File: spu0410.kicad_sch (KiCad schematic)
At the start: 10 parts, among them U1601 LT6233CS6#TRMPBF

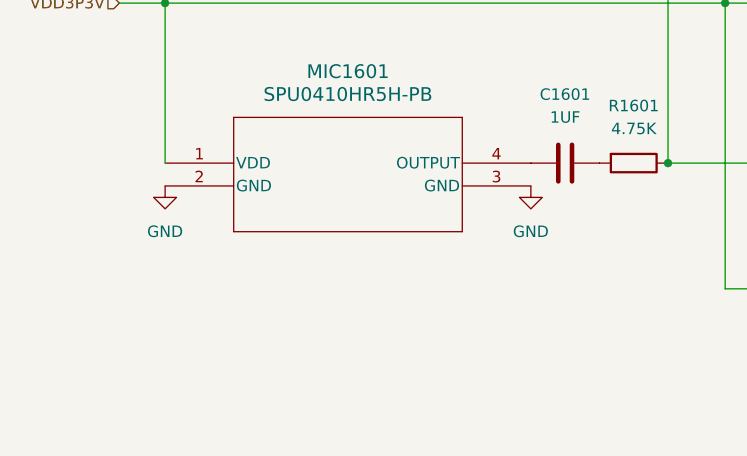
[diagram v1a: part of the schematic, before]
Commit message: Added -3.3V supply, buffer amplifier, and single-to-differential op-amp circuit
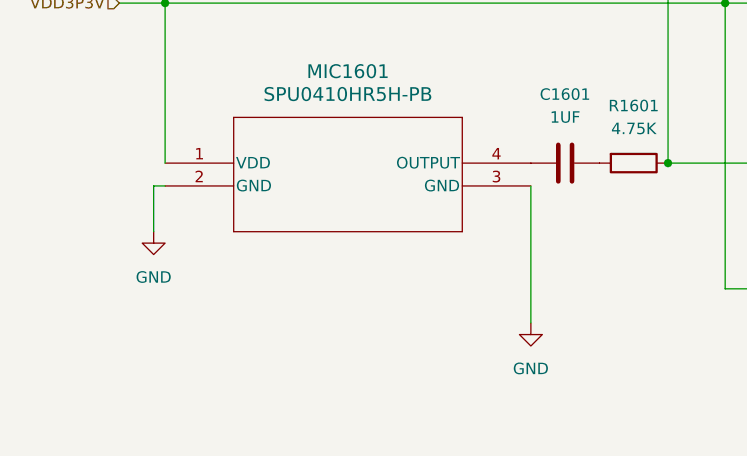
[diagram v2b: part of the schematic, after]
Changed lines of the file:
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@@
+	(wire
+		(pts
+			(xy 114.3 93.98) (xy 114.3 78.74)
+		)
+		(stroke
+			(width 0)
+			(type default)
+		)
+	)
 	(wire
 		(pts
@@
 	(wire
 		(pts
+			(xy 72.39 78.74) (xy 73.66 78.74)
+		)
+		(stroke
+			(width 0)
+			(type default)
+		)
+	)
+	(wire
+		(pts
 			(xy 209.55 73.66) (xy 209.55 74.93)
+		)
+		(stroke
+			(width 0)
+			(type default)
+		)
+	)
+	(wire
+		(pts
+			(xy 72.39 83.82) (xy 72.39 78.74)
 		)
 		(stroke
@@
 	(symbol
 		(lib_id "power:GND")
-		(at 73.66 78.74 0)
+		(at 72.39 83.82 0)
 		(unit 1)
 		(exclude_from_sim no)
@@
 		(fields_autoplaced yes)
 		(property "Reference" "#PWR01601"
-			(at 73.66 85.09 0)
+			(at 72.39 90.17 0)
 			(effects
 				(font
@@
 		)
 		(property "Value" "GND"
-			(at 73.66 83.82 0)
+			(at 72.39 88.9 0)
 			(effects
 				(font
@@
 		)
 		(property "Footprint" ""
-			(at 73.66 78.74 0)
+			(at 72.39 83.82 0)
 			(effects
 				(font
@@
 		)
 		(property "Datasheet" ""
-			(at 73.66 78.74 0)
+			(at 72.39 83.82 0)
 			(effects
 				(font
@@
 		)
 		(property "Description" "Power symbol creates a global label with name \"GND\" , ground"
-			(at 73.66 78.74 0)
+			(at 72.39 83.82 0)
 			(effects
 				(font
@@
 	(symbol
 		(lib_id "power:GND")
-		(at 114.3 78.74 0)
+		(at 114.3 93.98 0)
 		(unit 1)
 		(exclude_from_sim no)
@@
 		(fields_autoplaced yes)
 		(property "Reference" "#PWR01602"
-			(at 114.3 85.09 0)
+			(at 114.3 100.33 0)
 			(effects
 				(font
@@
 		)
 		(property "Value" "GND"
-			(at 114.3 83.82 0)
+			(at 114.3 99.06 0)
 			(effects
 				(font
@@
 		)
 		(property "Footprint" ""
-			(at 114.3 78.74 0)
+			(at 114.3 93.98 0)
 			(effects
 				(font
@@
 		)
 		(property "Datasheet" ""
-			(at 114.3 78.74 0)
+			(at 114.3 93.98 0)
 			(effects
 				(font
@@
 		)
 		(property "Description" "Power symbol creates a global label with name \"GND\" , ground"
-			(at 114.3 78.74 0)
-			(effects
-				(font
+			(at 114.3 93.98 0)
+			(effects
+				(font
